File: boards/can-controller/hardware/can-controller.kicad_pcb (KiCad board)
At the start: 2 copper layers, 100 x 100 mm, 5 parts, among them J1 RPi_GPIO

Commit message: can-controller: draft floorplan (Dwgs.User) and edge plan
Connectors: USB-C (GCT USB4085, THT), 12 V MSTB 5.08, CAN1/2 MC 3.5 4p on
the right; relay 10p and analog 12p on the bottom; GPIO 2 x 8p on the
left. 12 V domain bottom right with the isolators on its boundary.

Co-Authored-By: Claude Opus 5.5 <noreply@anthropic.com>
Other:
- board text added: "12 V DOMAIN (CAN bus ground)"
- board text added: "12V IN MSTBA 5.08 2p"
- board text added: "3.3 V LDO (header 5 V)"
- board text added: "ANALOG: AI1-4 + GND x4, AO1-2 + GND x2 MC 3.5 12p"
- board text added: "CAN1 MC 3.5 4p"
- board text added: "CAN1 fuse, TVS, TERM jp"
- board text added: "CAN2 MC 3.5 4p"
- board text added: "CAN2 fuse, TVS, TERM jp"
- board text added: "CAN3/4 expansion header (unpopulated)"
- board text added: "GPIO 1-4 + GND MC 3.5 8p"
- board text added: "GPIO 5-8 + GND MC 3.5 8p (under MCC HAT)"
- board text added: "GPIO series R + clamps"
- board text added: "ISO1042 CAN1"
- board text added: "ISO1042 CAN2"
- board text added: "ISO6741 RLY1-4"
- board text added: "ISO6741 RLY5-8"
- board text added: "LOGIC DOMAIN (Pi ground, header 5 V)"
- board text added: "MCC HAT outline (stacked above)"
- board text added: "PIC32MK1024GPK064 TQFP-64 + crystal"
- board text added: "RELAY 1-8 + 2x 12V COM MC 3.5 10p"
- board text added: "ULN2803A + relay LEDs"
- board text added: "USB ESD, CC 5.1k"
- board text added: "USB-C GCT USB4085 (THT)"
- board text added: "analog: MCP3428 + dividers, DAC + MC34072, boost 15 V, AI/AO protection"
- board text added: "buck 12->5 (ISO bus sides)"
- board text added: "eFuse, TVS, rev. polarity"
- board text added: "opto 12V OK"

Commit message: can-controller: floorplan variant B (4 CAN, Cmts.User) and density estimate
Co-Authored-By: Claude Opus 5.5 <noreply@anthropic.com>
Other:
- board text added: "12 V"
- board text added: "12V IN top-entry MSTBV 5.08 2p"
- board text added: "3.3 V LDO"
- board text added: "ANALOG 12p AI1-4, AO1-2 + GND"
- board text added: "CAN3 MC 3.5 4p"
- board text added: "CAN4 MC 3.5 4p"
- board text added: "GPIO 1-4 MC 3.5 8p"
- board text added: "GPIO 5-8 MC 3.5 8p"
- board text added: "ISO1042 CAN3"
- board text added: "ISO1042 CAN4"
- board text added: "PIC32MK TQFP-64 + crystal"
- board text added: "PTC, TVS, rev-pol FET, buck 12->5"
- board text added: "USB ESD, CC"
- board text added: "USB-C USB4085"
- board text added: "VARIANT B: 4 x CAN (Cmts.User layer)"
- board text added: "analog in/out"
- board text added: "fuse, TVS, TERM jp"
- board text added: "opto 12V"
- board text added: "spare"

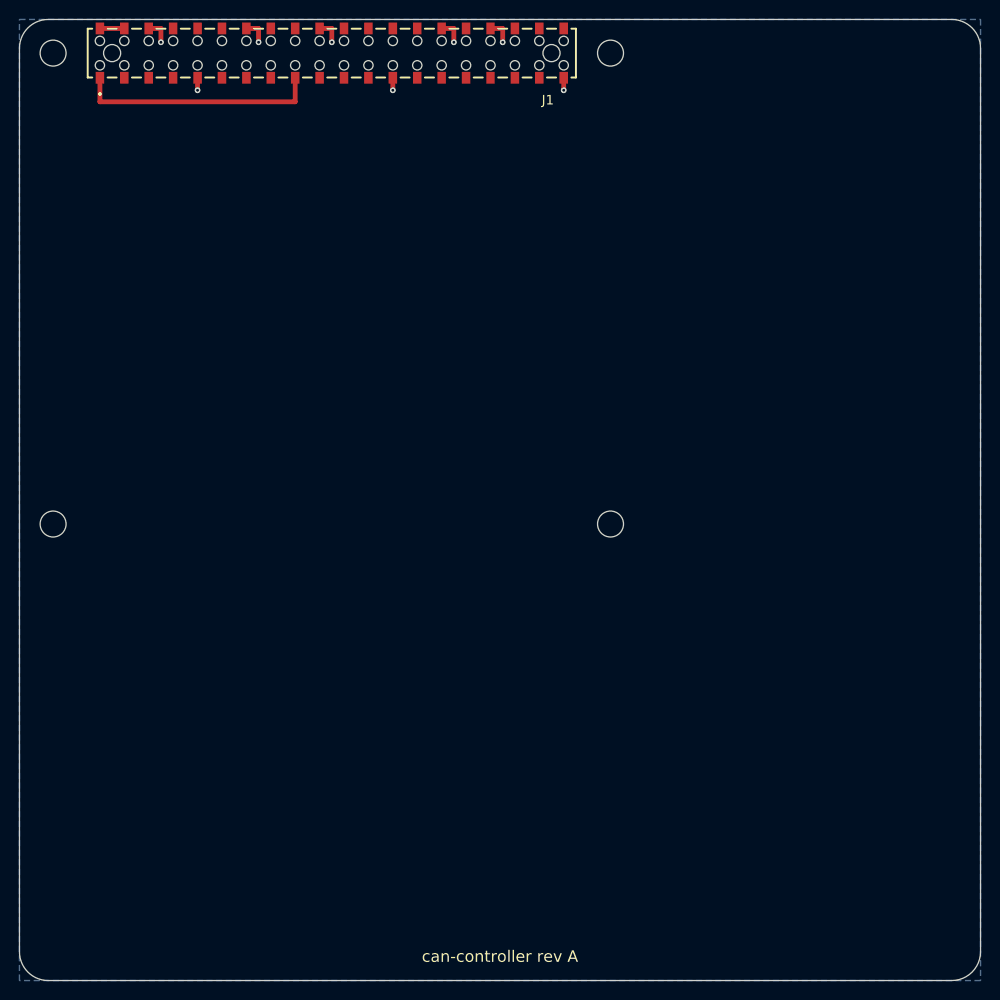
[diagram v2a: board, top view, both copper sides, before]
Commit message: can-controller: floorplan rev 2 (4 CAN), corner holes, DIN clips, draft parts
- Variant B adopted: USB-C + CAN4/3/1/2 on the right edge, 12 V input top
  entry inboard, relay 9p + analog 12p bottom, GPIO 2 x 8p left
- MH5-MH7 M2.5 in the other corners (93 mm square with MH1); DIN clip
  patterns MK1/MK2 at x 125 / 175, as on the first can-ssr layout
- DIN mount footprint: clip body courtyard on B.CrtYd only, 8 mm
  screw-head circles on F.CrtYd
- README: edge table, density estimate, draft parts list (ISO1044BD and
  ISO6740 proposed)

Co-Authored-By: Claude Opus 5.5 <noreply@anthropic.com>
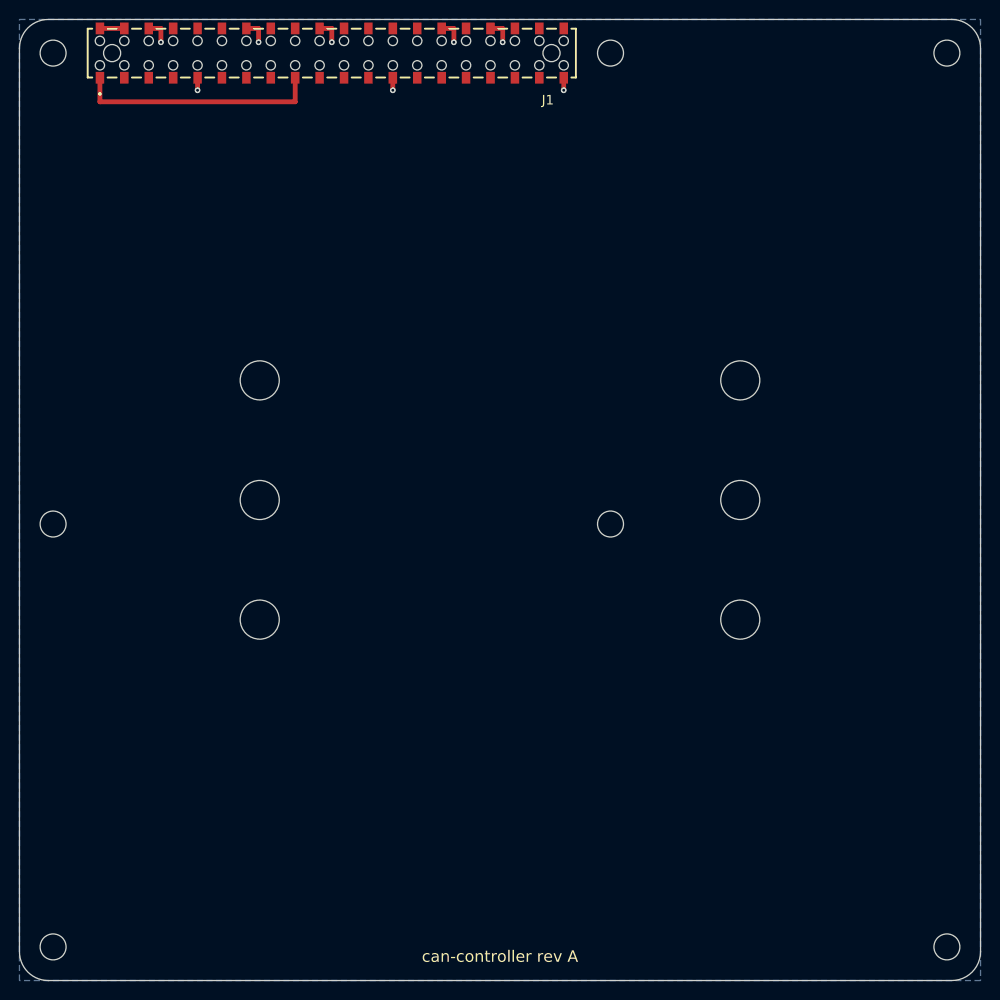
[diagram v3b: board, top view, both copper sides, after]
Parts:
- added MH5: MountingHole_2.7mm_M2.5, MountingHole:MountingHole_2.7mm_M2.5, F.Cu at (196.5, 103.5)
- added MH6: MountingHole_2.7mm_M2.5, MountingHole:MountingHole_2.7mm_M2.5, F.Cu at (103.5, 196.5)
- added MH7: MountingHole_2.7mm_M2.5, MountingHole:MountingHole_2.7mm_M2.5, F.Cu at (196.5, 196.5)
- added MK1: DIN rail clip, Thl_Mechanical:DIN_Rail_Mount_3xNPTH4.06mm_P12.45mm, F.Cu at (125.0, 150.0)
- added MK2: DIN rail clip, Thl_Mechanical:DIN_Rail_Mount_3xNPTH4.06mm_P12.45mm, F.Cu at (175.0, 150.0)
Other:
- board text added: "12 V DOMAIN"
- board text added: "12V IN top-entry MSTBVA 5.08 2p"
- board text added: "3.3 V LDO, ICSP, debug UART"
- board text added: "Floorplan rev 2 (variant B): 4 x CAN, corner holes MH5-7, DIN clips MK1/MK2"
- board text added: "GPIO 5-8 + GND MC 3.5 8p"
- board text added: "ISO1044 CAN1"
- board text added: "ISO1044 CAN2"
- board text added: "ISO1044 CAN3"
- board text added: "ISO1044 CAN4"
- board text added: "ISO6740 RLY1-4"
- board text added: "ISO6740 RLY5-8"
- board text added: "PTC, TVS, TERM jp"
- board text added: "RELAY 1-8 + 12V COM MC 3.5 9p"
- board text added: "ULN2803A SOIC-18W"
- board text added: "USB ESD, CC, LEDs"
- board text added: "analog: MCP3428 + dividers, DAC + op amps + 15 V boost, VREF, AI/AO protection"
- board text added: "buck 12->5"
- board text added: "fuse, TVS, rev-pol FET"
- board text added: "relay + CAN LEDs, 12V status, spare"
- board text removed: "12 V"
- board text removed: "12 V DOMAIN (CAN bus ground)"
- board text removed: "12V IN MSTBA 5.08 2p"
- board text removed: "12V IN top-entry MSTBV 5.08 2p"
- board text removed: "3.3 V LDO"
- board text removed: "3.3 V LDO (header 5 V)"
- board text removed: "ANALOG 12p AI1-4, AO1-2 + GND"
- board text removed: "CAN1 fuse, TVS, TERM jp"
- board text removed: "CAN2 fuse, TVS, TERM jp"
- board text removed: "CAN3/4 expansion header (unpopulated)"
- board text removed: "GPIO 1-4 MC 3.5 8p"
- board text removed: "GPIO 5-8 + GND MC 3.5 8p (under MCC HAT)"
- board text removed: "GPIO 5-8 MC 3.5 8p"
- board text removed: "ISO1042 CAN1"
- board text removed: "ISO1042 CAN2"
- board text removed: "ISO1042 CAN3"
- board text removed: "ISO1042 CAN4"
- board text removed: "ISO6741 RLY1-4"
- board text removed: "ISO6741 RLY5-8"
- board text removed: "MCC HAT outline (stacked above)"
- board text removed: "PIC32MK TQFP-64 + crystal"
- board text removed: "PTC, TVS, rev-pol FET, buck 12->5"
- board text removed: "RELAY 1-8 + 2x 12V COM MC 3.5 10p"
- board text removed: "ULN2803A + relay LEDs"
- board text removed: "USB ESD, CC"
- board text removed: "USB ESD, CC 5.1k"
- board text removed: "USB-C GCT USB4085 (THT)"
- board text removed: "VARIANT B: 4 x CAN (Cmts.User layer)"
- board text removed: "analog in/out"
- board text removed: "analog: MCP3428 + dividers, DAC + MC34072, boost 15 V, AI/AO protection"
- board text removed: "buck 12->5 (ISO bus sides)"
- board text removed: "eFuse, TVS, rev. polarity"
- board text removed: "fuse, TVS, TERM jp"
- board text removed: "opto 12V"
- board text removed: "spare"

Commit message: can-controller: first schematic capture (7 sheets), footprints parked
- gen_schematic.py (first capture only, like can-ssr's): MCU/USB/power,
  CAN x4 (ISO1044BD; +12 V fuse fitted on CAN1, DNP on CAN2-4), 12 V input
  (NANO2 fuse, SUD50P04-08 reverse-polarity P-FET, SMBJ15A, R-78E 5 V for
  the bus sides, TLP293 12 V status), relay drive (2 x ISO6740, ULN2803A,
  logic-side LEDs), GPIO (8 x 4.7k + BAT54S), analog in (MCP3428, dividers
  referenced to VMID because the ADC cannot go below VSS), analog out
  (MCP4922 + LM4040 2.5 V, LM358B gain 4 on a 13 V TPS61040 boost,
  470R + 15 V Zener output protection)
- MCU pin map checked against the PPS group tables of DS60001519E
- ERC 0, parity clean; only isolators span the two domains
- PCB: footprints synced and parked; template copper removed
- sync_pcb.py now carries the DNP attribute to the PCB
- House DRC rule: 0.15 mm annular ring for the GCT USB4085 only
- 3D models for SOIC-4 (SOP-4) and the 1812 PTC (C_1812 stand-in)

Co-Authored-By: Claude Opus 5.5 <noreply@anthropic.com>
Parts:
- added C1: 10uF 25V X7R, Capacitor_SMD:C_1206_3216Metric_Pad1.33x1.80mm_HandSolder, F.Cu at (220.0, 100.0)
- added C10: 27pF 50V C0G, Capacitor_SMD:C_0805_2012Metric_Pad1.18x1.45mm_HandSolder, F.Cu at (245.0, 100.0)
- added C11: 27pF 50V C0G, Capacitor_SMD:C_0805_2012Metric_Pad1.18x1.45mm_HandSolder, F.Cu at (270.0, 100.0)
- added C12: 100nF 50V X7R, Capacitor_SMD:C_0805_2012Metric_Pad1.18x1.45mm_HandSolder, F.Cu at (295.0, 100.0)
- added C2: 10uF 25V X7R, Capacitor_SMD:C_1206_3216Metric_Pad1.33x1.80mm_HandSolder, F.Cu at (320.0, 100.0)
- added C20: 100nF 50V X7R, Capacitor_SMD:C_0805_2012Metric_Pad1.18x1.45mm_HandSolder, F.Cu at (345.0, 100.0)
- added C21: 100nF 50V X7R, Capacitor_SMD:C_0805_2012Metric_Pad1.18x1.45mm_HandSolder, F.Cu at (370.0, 100.0)
- added C22: 100nF 50V X7R, Capacitor_SMD:C_0805_2012Metric_Pad1.18x1.45mm_HandSolder, F.Cu at (395.0, 100.0)
- added C23: 100nF 50V X7R, Capacitor_SMD:C_0805_2012Metric_Pad1.18x1.45mm_HandSolder, F.Cu at (420.0, 100.0)
- added C24: 100nF 50V X7R, Capacitor_SMD:C_0805_2012Metric_Pad1.18x1.45mm_HandSolder, F.Cu at (445.0, 100.0)
- added C25: 100nF 50V X7R, Capacitor_SMD:C_0805_2012Metric_Pad1.18x1.45mm_HandSolder, F.Cu at (220.0, 125.0)
- added C26: 100nF 50V X7R, Capacitor_SMD:C_0805_2012Metric_Pad1.18x1.45mm_HandSolder, F.Cu at (245.0, 125.0)
- added C27: 100nF 50V X7R, Capacitor_SMD:C_0805_2012Metric_Pad1.18x1.45mm_HandSolder, F.Cu at (270.0, 125.0)
- added C3: 100nF 50V X7R, Capacitor_SMD:C_0805_2012Metric_Pad1.18x1.45mm_HandSolder, F.Cu at (295.0, 125.0)
- added C30: 10uF 25V X7R, Capacitor_SMD:C_1206_3216Metric_Pad1.33x1.80mm_HandSolder, F.Cu at (320.0, 125.0)
- added C31: 10uF 25V X7R, Capacitor_SMD:C_1206_3216Metric_Pad1.33x1.80mm_HandSolder, F.Cu at (345.0, 125.0)
- added C32: 10uF 25V X7R, Capacitor_SMD:C_1206_3216Metric_Pad1.33x1.80mm_HandSolder, F.Cu at (370.0, 125.0)
- added C4: 100nF 50V X7R, Capacitor_SMD:C_0805_2012Metric_Pad1.18x1.45mm_HandSolder, F.Cu at (395.0, 125.0)
- added C40: 100nF 50V X7R, Capacitor_SMD:C_0805_2012Metric_Pad1.18x1.45mm_HandSolder, F.Cu at (420.0, 125.0)
- added C41: 100nF 50V X7R, Capacitor_SMD:C_0805_2012Metric_Pad1.18x1.45mm_HandSolder, F.Cu at (445.0, 125.0)
- added C42: 100nF 50V X7R, Capacitor_SMD:C_0805_2012Metric_Pad1.18x1.45mm_HandSolder, F.Cu at (220.0, 150.0)
- added C43: 100nF 50V X7R, Capacitor_SMD:C_0805_2012Metric_Pad1.18x1.45mm_HandSolder, F.Cu at (245.0, 150.0)
- added C44: 10uF 25V X7R, Capacitor_SMD:C_1206_3216Metric_Pad1.33x1.80mm_HandSolder, F.Cu at (270.0, 150.0)
- added C5: 100nF 50V X7R, Capacitor_SMD:C_0805_2012Metric_Pad1.18x1.45mm_HandSolder, F.Cu at (295.0, 150.0)
- added C50: 100nF 50V X7R, Capacitor_SMD:C_0805_2012Metric_Pad1.18x1.45mm_HandSolder, F.Cu at (320.0, 150.0)
- added C51: 10uF 25V X7R, Capacitor_SMD:C_1206_3216Metric_Pad1.33x1.80mm_HandSolder, F.Cu at (345.0, 150.0)
- added C52: 100nF 50V X7R, Capacitor_SMD:C_1206_3216Metric_Pad1.33x1.80mm_HandSolder, F.Cu at (370.0, 150.0)
- added C53: 100nF 50V X7R, Capacitor_SMD:C_1206_3216Metric_Pad1.33x1.80mm_HandSolder, F.Cu at (395.0, 150.0)
- added C54: 100nF 50V X7R, Capacitor_SMD:C_1206_3216Metric_Pad1.33x1.80mm_HandSolder, F.Cu at (420.0, 150.0)
- added C55: 100nF 50V X7R, Capacitor_SMD:C_1206_3216Metric_Pad1.33x1.80mm_HandSolder, F.Cu at (445.0, 150.0)
- added C6: 100nF 50V X7R, Capacitor_SMD:C_0805_2012Metric_Pad1.18x1.45mm_HandSolder, F.Cu at (220.0, 175.0)
- added C60: 100nF 50V X7R, Capacitor_SMD:C_0805_2012Metric_Pad1.18x1.45mm_HandSolder, F.Cu at (245.0, 175.0)
- added C61: 100nF 50V X7R, Capacitor_SMD:C_0805_2012Metric_Pad1.18x1.45mm_HandSolder, F.Cu at (270.0, 175.0)
- added C62: 100nF 50V X7R, Capacitor_SMD:C_0805_2012Metric_Pad1.18x1.45mm_HandSolder, F.Cu at (295.0, 175.0)
- added C63: 4.7uF 25V X7R, Capacitor_SMD:C_1206_3216Metric_Pad1.33x1.80mm_HandSolder, F.Cu at (320.0, 175.0)
- added C64: 10uF 25V X7R, Capacitor_SMD:C_1206_3216Metric_Pad1.33x1.80mm_HandSolder, F.Cu at (345.0, 175.0)
- added C7: 10uF 25V X7R, Capacitor_SMD:C_1206_3216Metric_Pad1.33x1.80mm_HandSolder, F.Cu at (370.0, 175.0)
- added C8: 100nF 50V X7R, Capacitor_SMD:C_0805_2012Metric_Pad1.18x1.45mm_HandSolder, F.Cu at (395.0, 175.0)
- added C9: 100nF 50V X7R, Capacitor_SMD:C_0805_2012Metric_Pad1.18x1.45mm_HandSolder, F.Cu at (420.0, 175.0)
- added D1: LED green, LED_SMD:LED_1206_3216Metric_Pad1.42x1.75mm_HandSolder, F.Cu at (445.0, 175.0)
- added D10: 15V, Diode_SMD:D_SOD-123, F.Cu at (220.0, 200.0)
- added D11: SMBJ15A, Diode_SMD:D_SMB_Handsoldering, F.Cu at (245.0, 200.0)
- added D12: LED green, LED_SMD:LED_1206_3216Metric_Pad1.42x1.75mm_HandSolder, F.Cu at (270.0, 200.0)
- added D2: LED green, LED_SMD:LED_1206_3216Metric_Pad1.42x1.75mm_HandSolder, F.Cu at (295.0, 200.0)
- added D20: NUP2105L, Package_TO_SOT_SMD:SOT-23, F.Cu at (320.0, 200.0)
- added D21: NUP2105L, Package_TO_SOT_SMD:SOT-23, F.Cu at (345.0, 200.0)
- added D22: NUP2105L, Package_TO_SOT_SMD:SOT-23, F.Cu at (370.0, 200.0)
- added D23: NUP2105L, Package_TO_SOT_SMD:SOT-23, F.Cu at (395.0, 200.0)
- added D24: LED yellow, LED_SMD:LED_1206_3216Metric_Pad1.42x1.75mm_HandSolder, F.Cu at (420.0, 200.0)
- added D25: LED yellow, LED_SMD:LED_1206_3216Metric_Pad1.42x1.75mm_HandSolder, F.Cu at (445.0, 200.0)
- added D26: LED yellow, LED_SMD:LED_1206_3216Metric_Pad1.42x1.75mm_HandSolder, F.Cu at (220.0, 225.0)
- added D27: LED yellow, LED_SMD:LED_1206_3216Metric_Pad1.42x1.75mm_HandSolder, F.Cu at (245.0, 225.0)
- added D3: LED green, LED_SMD:LED_1206_3216Metric_Pad1.42x1.75mm_HandSolder, F.Cu at (270.0, 225.0)
- added D31: LED red, LED_SMD:LED_1206_3216Metric_Pad1.42x1.75mm_HandSolder, F.Cu at (295.0, 225.0)
- added D32: LED red, LED_SMD:LED_1206_3216Metric_Pad1.42x1.75mm_HandSolder, F.Cu at (320.0, 225.0)
- added D33: LED red, LED_SMD:LED_1206_3216Metric_Pad1.42x1.75mm_HandSolder, F.Cu at (345.0, 225.0)
- added D34: LED red, LED_SMD:LED_1206_3216Metric_Pad1.42x1.75mm_HandSolder, F.Cu at (370.0, 225.0)
- added D35: LED red, LED_SMD:LED_1206_3216Metric_Pad1.42x1.75mm_HandSolder, F.Cu at (395.0, 225.0)
- added D36: LED red, LED_SMD:LED_1206_3216Metric_Pad1.42x1.75mm_HandSolder, F.Cu at (420.0, 225.0)
- added D37: LED red, LED_SMD:LED_1206_3216Metric_Pad1.42x1.75mm_HandSolder, F.Cu at (445.0, 225.0)
- added D38: LED red, LED_SMD:LED_1206_3216Metric_Pad1.42x1.75mm_HandSolder, F.Cu at (220.0, 250.0)
- added D51: BAT54S, Package_TO_SOT_SMD:SOT-23, F.Cu at (245.0, 250.0)
- added D52: BAT54S, Package_TO_SOT_SMD:SOT-23, F.Cu at (270.0, 250.0)
- added D53: BAT54S, Package_TO_SOT_SMD:SOT-23, F.Cu at (295.0, 250.0)
- added D54: BAT54S, Package_TO_SOT_SMD:SOT-23, F.Cu at (320.0, 250.0)
- added D55: BAT54S, Package_TO_SOT_SMD:SOT-23, F.Cu at (345.0, 250.0)
- added D56: BAT54S, Package_TO_SOT_SMD:SOT-23, F.Cu at (370.0, 250.0)
- added D57: BAT54S, Package_TO_SOT_SMD:SOT-23, F.Cu at (395.0, 250.0)
- added D58: BAT54S, Package_TO_SOT_SMD:SOT-23, F.Cu at (420.0, 250.0)
- added D61: BAT54S, Package_TO_SOT_SMD:SOT-23, F.Cu at (445.0, 250.0)
- added D62: BAT54S, Package_TO_SOT_SMD:SOT-23, F.Cu at (220.0, 275.0)
- added D63: BAT54S, Package_TO_SOT_SMD:SOT-23, F.Cu at (245.0, 275.0)
- added D64: BAT54S, Package_TO_SOT_SMD:SOT-23, F.Cu at (270.0, 275.0)
- added D71: 15V, Diode_SMD:D_SOD-123, F.Cu at (295.0, 275.0)
- added D72: 15V, Diode_SMD:D_SOD-123, F.Cu at (320.0, 275.0)
- added D73: MBR0530, Diode_SMD:D_SOD-123, F.Cu at (345.0, 275.0)
- added F1: 0.75A, Fuse:Fuse_1206_3216Metric_Pad1.42x1.75mm_HandSolder, F.Cu at (370.0, 275.0)
- added F10: 1.1A, Fuse:Fuse_1812_4532Metric_Pad1.30x3.40mm_HandSolder, F.Cu at (395.0, 275.0)
- added F11: 1.1A, Fuse:Fuse_1812_4532Metric_Pad1.30x3.40mm_HandSolder, F.Cu at (420.0, 275.0)
- added F12: 1.1A, Fuse:Fuse_1812_4532Metric_Pad1.30x3.40mm_HandSolder, F.Cu at (445.0, 275.0)
- added F13: 1.1A, Fuse:Fuse_1812_4532Metric_Pad1.30x3.40mm_HandSolder, F.Cu at (220.0, 300.0)
- added F20: 4A, Fuse:Fuse_Littelfuse-NANO2-451_453, F.Cu at (245.0, 300.0)
- added F30: 1.1A, Fuse:Fuse_1812_4532Metric_Pad1.30x3.40mm_HandSolder, F.Cu at (270.0, 300.0)
- added FB1: 600R@100MHz, Inductor_SMD:L_0805_2012Metric_Pad1.05x1.20mm_HandSolder, F.Cu at (295.0, 300.0)
- added J10: CAN1, Connector_Phoenix_MC:PhoenixContact_MC_1,5_4-G-3.5_1x04_P3.50mm_Horizontal, F.Cu at (320.0, 300.0)
- added J11: CAN2, Connector_Phoenix_MC:PhoenixContact_MC_1,5_4-G-3.5_1x04_P3.50mm_Horizontal, F.Cu at (345.0, 300.0)
- added J12: CAN3, Connector_Phoenix_MC:PhoenixContact_MC_1,5_4-G-3.5_1x04_P3.50mm_Horizontal, F.Cu at (370.0, 300.0)
- added J13: CAN4, Connector_Phoenix_MC:PhoenixContact_MC_1,5_4-G-3.5_1x04_P3.50mm_Horizontal, F.Cu at (395.0, 300.0)
- added J2: ICSP, Connector_PinHeader_2.54mm:PinHeader_1x06_P2.54mm_Vertical, F.Cu at (420.0, 300.0)
- added J20: 12V IN, Connector_Phoenix_MSTB:PhoenixContact_MSTBVA_2,5_2-G-5,08_1x02_P5.08mm_Vertical, F.Cu at (445.0, 300.0)
- added J3: UART, Connector_PinHeader_2.54mm:PinHeader_1x03_P2.54mm_Vertical, F.Cu at (220.0, 325.0)
- added J30: RELAY, Connector_Phoenix_MC:PhoenixContact_MC_1,5_9-G-3.5_1x09_P3.50mm_Horizontal, F.Cu at (245.0, 325.0)
- added J4: USB-C, Connector_USB:USB_C_Receptacle_GCT_USB4085, F.Cu at (270.0, 325.0)
- added J40: GPIO 1-4, Connector_Phoenix_MC:PhoenixContact_MC_1,5_8-G-3.5_1x08_P3.50mm_Horizontal, F.Cu at (295.0, 325.0)
- added J41: GPIO 5-8, Connector_Phoenix_MC:PhoenixContact_MC_1,5_8-G-3.5_1x08_P3.50mm_Horizontal, F.Cu at (320.0, 325.0)
- added J50: ANALOG, Connector_Phoenix_MC:PhoenixContact_MC_1,5_12-G-3.5_1x12_P3.50mm_Horizontal, F.Cu at (345.0, 325.0)
- added JP1: TERM, Connector_PinHeader_2.54mm:PinHeader_1x02_P2.54mm_Vertical, F.Cu at (370.0, 325.0)
- added JP2: TERM, Connector_PinHeader_2.54mm:PinHeader_1x02_P2.54mm_Vertical, F.Cu at (395.0, 325.0)
- added JP3: TERM, Connector_PinHeader_2.54mm:PinHeader_1x02_P2.54mm_Vertical, F.Cu at (420.0, 325.0)
- added JP4: TERM, Connector_PinHeader_2.54mm:PinHeader_1x02_P2.54mm_Vertical, F.Cu at (445.0, 325.0)
- added L60: 10uH, Inductor_SMD:L_Bourns-SRN4018, F.Cu at (220.0, 350.0)
- added Q1: SUD50P04-08, Package_TO_SOT_SMD:TO-252-2, F.Cu at (245.0, 350.0)
- added R1: 1k, Resistor_SMD:R_1206_3216Metric_Pad1.30x1.75mm_HandSolder, F.Cu at (270.0, 350.0)
- added R2: 10k, Resistor_SMD:R_1206_3216Metric_Pad1.30x1.75mm_HandSolder, F.Cu at (295.0, 350.0)
- added R20: 120R, Resistor_SMD:R_1206_3216Metric_Pad1.30x1.75mm_HandSolder, F.Cu at (320.0, 350.0)
- added R21: 120R, Resistor_SMD:R_1206_3216Metric_Pad1.30x1.75mm_HandSolder, F.Cu at (345.0, 350.0)
- added R22: 120R, Resistor_SMD:R_1206_3216Metric_Pad1.30x1.75mm_HandSolder, F.Cu at (370.0, 350.0)
- added R23: 120R, Resistor_SMD:R_1206_3216Metric_Pad1.30x1.75mm_HandSolder, F.Cu at (395.0, 350.0)
- added R24: 1k, Resistor_SMD:R_1206_3216Metric_Pad1.30x1.75mm_HandSolder, F.Cu at (420.0, 350.0)
- added R25: 1k, Resistor_SMD:R_1206_3216Metric_Pad1.30x1.75mm_HandSolder, F.Cu at (445.0, 350.0)
- added R26: 1k, Resistor_SMD:R_1206_3216Metric_Pad1.30x1.75mm_HandSolder, F.Cu at (220.0, 375.0)
- added R27: 1k, Resistor_SMD:R_1206_3216Metric_Pad1.30x1.75mm_HandSolder, F.Cu at (245.0, 375.0)
- added R3: 5.1k, Resistor_SMD:R_1206_3216Metric_Pad1.30x1.75mm_HandSolder, F.Cu at (270.0, 375.0)
- added R30: 10k, Resistor_SMD:R_1206_3216Metric_Pad1.30x1.75mm_HandSolder, F.Cu at (295.0, 375.0)
- added R31: 4.7k, Resistor_SMD:R_1206_3216Metric_Pad1.30x1.75mm_HandSolder, F.Cu at (320.0, 375.0)
- added R32: 10k, Resistor_SMD:R_1206_3216Metric_Pad1.30x1.75mm_HandSolder, F.Cu at (345.0, 375.0)
- added R33: 10k, Resistor_SMD:R_1206_3216Metric_Pad1.30x1.75mm_HandSolder, F.Cu at (370.0, 375.0)
- added R34: 1k, Resistor_SMD:R_1206_3216Metric_Pad1.30x1.75mm_HandSolder, F.Cu at (395.0, 375.0)
- added R4: 5.1k, Resistor_SMD:R_1206_3216Metric_Pad1.30x1.75mm_HandSolder, F.Cu at (420.0, 375.0)
- added R41: 1k, Resistor_SMD:R_1206_3216Metric_Pad1.30x1.75mm_HandSolder, F.Cu at (445.0, 375.0)
- added R42: 1k, Resistor_SMD:R_1206_3216Metric_Pad1.30x1.75mm_HandSolder, F.Cu at (220.0, 400.0)
- added R43: 1k, Resistor_SMD:R_1206_3216Metric_Pad1.30x1.75mm_HandSolder, F.Cu at (245.0, 400.0)
- added R44: 1k, Resistor_SMD:R_1206_3216Metric_Pad1.30x1.75mm_HandSolder, F.Cu at (270.0, 400.0)
- added R45: 1k, Resistor_SMD:R_1206_3216Metric_Pad1.30x1.75mm_HandSolder, F.Cu at (295.0, 400.0)
- added R46: 1k, Resistor_SMD:R_1206_3216Metric_Pad1.30x1.75mm_HandSolder, F.Cu at (320.0, 400.0)
- added R47: 1k, Resistor_SMD:R_1206_3216Metric_Pad1.30x1.75mm_HandSolder, F.Cu at (345.0, 400.0)
- added R48: 1k, Resistor_SMD:R_1206_3216Metric_Pad1.30x1.75mm_HandSolder, F.Cu at (370.0, 400.0)
- added R5: 1k, Resistor_SMD:R_1206_3216Metric_Pad1.30x1.75mm_HandSolder, F.Cu at (395.0, 400.0)
- added R51: 4.7k, Resistor_SMD:R_1206_3216Metric_Pad1.30x1.75mm_HandSolder, F.Cu at (420.0, 400.0)
- added R52: 4.7k, Resistor_SMD:R_1206_3216Metric_Pad1.30x1.75mm_HandSolder, F.Cu at (445.0, 400.0)
- added R53: 4.7k, Resistor_SMD:R_1206_3216Metric_Pad1.30x1.75mm_HandSolder, F.Cu at (220.0, 425.0)
- added R54: 4.7k, Resistor_SMD:R_1206_3216Metric_Pad1.30x1.75mm_HandSolder, F.Cu at (245.0, 425.0)
- added R55: 4.7k, Resistor_SMD:R_1206_3216Metric_Pad1.30x1.75mm_HandSolder, F.Cu at (270.0, 425.0)
- added R56: 4.7k, Resistor_SMD:R_1206_3216Metric_Pad1.30x1.75mm_HandSolder, F.Cu at (295.0, 425.0)
- added R57: 4.7k, Resistor_SMD:R_1206_3216Metric_Pad1.30x1.75mm_HandSolder, F.Cu at (320.0, 425.0)
- added R58: 4.7k, Resistor_SMD:R_1206_3216Metric_Pad1.30x1.75mm_HandSolder, F.Cu at (345.0, 425.0)
- added R6: 100k, Resistor_SMD:R_1206_3216Metric_Pad1.30x1.75mm_HandSolder, F.Cu at (370.0, 425.0)
- added R60: 4.7k, Resistor_SMD:R_1206_3216Metric_Pad1.30x1.75mm_HandSolder, F.Cu at (395.0, 425.0)
- added R61: 4.7k, Resistor_SMD:R_1206_3216Metric_Pad1.30x1.75mm_HandSolder, F.Cu at (420.0, 425.0)
- added R62: 10k, Resistor_SMD:R_1206_3216Metric_Pad1.30x1.75mm_HandSolder, F.Cu at (445.0, 425.0)
- added R63: 10k, Resistor_SMD:R_1206_3216Metric_Pad1.30x1.75mm_HandSolder, F.Cu at (220.0, 450.0)
- added R64: 10M, Resistor_SMD:R_1206_3216Metric_Pad1.30x1.75mm_HandSolder, F.Cu at (245.0, 450.0)
- added R65: 10M, Resistor_SMD:R_1206_3216Metric_Pad1.30x1.75mm_HandSolder, F.Cu at (270.0, 450.0)
- added R66: 10M, Resistor_SMD:R_1206_3216Metric_Pad1.30x1.75mm_HandSolder, F.Cu at (295.0, 450.0)
- added R67: 10M, Resistor_SMD:R_1206_3216Metric_Pad1.30x1.75mm_HandSolder, F.Cu at (320.0, 450.0)
- added R68: 130k, Resistor_SMD:R_1206_3216Metric_Pad1.30x1.75mm_HandSolder, F.Cu at (345.0, 450.0)
- added R69: 130k, Resistor_SMD:R_1206_3216Metric_Pad1.30x1.75mm_HandSolder, F.Cu at (370.0, 450.0)
- added R7: 1k, Resistor_SMD:R_1206_3216Metric_Pad1.30x1.75mm_HandSolder, F.Cu at (395.0, 450.0)
- added R70: 130k, Resistor_SMD:R_1206_3216Metric_Pad1.30x1.75mm_HandSolder, F.Cu at (420.0, 450.0)
- added R71: 130k, Resistor_SMD:R_1206_3216Metric_Pad1.30x1.75mm_HandSolder, F.Cu at (445.0, 450.0)
- added R8: 1k, Resistor_SMD:R_1206_3216Metric_Pad1.30x1.75mm_HandSolder, F.Cu at (345.0, 475.0)
- added R80: 1k, Resistor_SMD:R_1206_3216Metric_Pad1.30x1.75mm_HandSolder, F.Cu at (370.0, 475.0)
- added R81: 470R, Resistor_SMD:R_1206_3216Metric_Pad1.30x1.75mm_HandSolder, F.Cu at (395.0, 475.0)
- added R82: 30k, Resistor_SMD:R_1206_3216Metric_Pad1.30x1.75mm_HandSolder, F.Cu at (220.0, 100.0)
- added R83: 10k, Resistor_SMD:R_1206_3216Metric_Pad1.30x1.75mm_HandSolder, F.Cu at (245.0, 100.0)
- added R85: 470R, Resistor_SMD:R_1206_3216Metric_Pad1.30x1.75mm_HandSolder, F.Cu at (270.0, 100.0)
- added R86: 30k, Resistor_SMD:R_1206_3216Metric_Pad1.30x1.75mm_HandSolder, F.Cu at (295.0, 100.0)
- added R87: 10k, Resistor_SMD:R_1206_3216Metric_Pad1.30x1.75mm_HandSolder, F.Cu at (320.0, 100.0)
- added R90: 1M, Resistor_SMD:R_1206_3216Metric_Pad1.30x1.75mm_HandSolder, F.Cu at (345.0, 100.0)
- added R91: 105k, Resistor_SMD:R_1206_3216Metric_Pad1.30x1.75mm_HandSolder, F.Cu at (370.0, 100.0)
- added U1: PIC32MK1024MCM064-I/PT, Package_QFP:TQFP-64_10x10mm_P0.5mm, F.Cu at (420.0, 475.0)
- added U10: ISO1044BD, Package_SO:SOIC-8_3.9x4.9mm_P1.27mm, F.Cu at (445.0, 475.0)
- added U11: ISO1044BD, Package_SO:SOIC-8_3.9x4.9mm_P1.27mm, F.Cu at (220.0, 500.0)
- added U12: ISO1044BD, Package_SO:SOIC-8_3.9x4.9mm_P1.27mm, F.Cu at (245.0, 500.0)
- added U13: ISO1044BD, Package_SO:SOIC-8_3.9x4.9mm_P1.27mm, F.Cu at (270.0, 500.0)
- added U2: MCP1826S-3302E/DB, Package_TO_SOT_SMD:SOT-223-3_TabPin2, F.Cu at (295.0, 500.0)
- added U20: R-78E5.0-0.5, Converter_DCDC:Converter_DCDC_RECOM_R-78E-0.5_THT, F.Cu at (320.0, 500.0)
- added U21: TLP293, Package_SO:SOIC-4_4.55x2.6mm_P1.27mm, F.Cu at (345.0, 500.0)
- added U3: USBLC6-2SC6, Package_TO_SOT_SMD:SOT-23-6, F.Cu at (370.0, 500.0)
- added U30: ISO6740, Package_SO:SOIC-16W_7.5x10.3mm_P1.27mm, F.Cu at (395.0, 500.0)
- added U31: ISO6740, Package_SO:SOIC-16W_7.5x10.3mm_P1.27mm, F.Cu at (420.0, 500.0)
- added U32: ULN2803A, Package_SO:SOIC-18W_7.5x11.6mm_P1.27mm, F.Cu at (445.0, 500.0)
- added U50: MCP3428-E/SL, Package_SO:SOIC-14_3.9x8.7mm_P1.27mm, F.Cu at (220.0, 525.0)
- added U60: MCP4922-E/SL, Package_SO:SOIC-14_3.9x8.7mm_P1.27mm, F.Cu at (245.0, 525.0)
- added U61: LM4040-2.5, Package_TO_SOT_SMD:SOT-23, F.Cu at (270.0, 525.0)
- added U62: LM358B, Package_SO:SOIC-8_3.9x4.9mm_P1.27mm, F.Cu at (295.0, 525.0)
- added U63: TPS61040, Package_TO_SOT_SMD:SOT-23-5, F.Cu at (320.0, 525.0)
- added Y1: 12MHz, Crystal:Crystal_SMD_5032-2Pin_5.0x3.2mm_HandSoldering, F.Cu at (345.0, 525.0)
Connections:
- net +5V renamed /MCU, USB, power/V5_PI
- J1 pad 1: +3.3V -> unconnected-(J1-Pin_1-Pad1)
- J1 pad 10: /GPIO15_RXD -> unconnected-(J1-Pin_10-Pad10)
- J1 pad 11: /GPIO17 -> unconnected-(J1-Pin_11-Pad11)
- J1 pad 12: /GPIO18_PCM_CLK -> unconnected-(J1-Pin_12-Pad12)
- J1 pad 13: /GPIO27 -> unconnected-(J1-Pin_13-Pad13)
- J1 pad 15: /GPIO22 -> unconnected-(J1-Pin_15-Pad15)
- J1 pad 16: /GPIO23 -> unconnected-(J1-Pin_16-Pad16)
- J1 pad 17: +3.3V -> unconnected-(J1-Pin_17-Pad17)
- J1 pad 18: /GPIO24 -> unconnected-(J1-Pin_18-Pad18)
- J1 pad 22: /GPIO25 -> unconnected-(J1-Pin_22-Pad22)
- J1 pad 29: /GPIO5 -> unconnected-(J1-Pin_29-Pad29)
- J1 pad 3: /GPIO2_SDA -> unconnected-(J1-Pin_3-Pad3)
- J1 pad 31: /GPIO6 -> unconnected-(J1-Pin_31-Pad31)
- J1 pad 35: /GPIO19_PCM_FS -> unconnected-(J1-Pin_35-Pad35)
- J1 pad 5: /GPIO3_SCL -> unconnected-(J1-Pin_5-Pad5)
- J1 pad 7: /GPIO4_GPCLK0 -> unconnected-(J1-Pin_7-Pad7)
- J1 pad 8: /GPIO14_TXD -> unconnected-(J1-Pin_8-Pad8)
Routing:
- net +3.3V: track 25.3 -> 0.00 mm
- net GND: track 17.5 -> 0.00 mm, vias 8 -> 0
- net /MCU, USB, power/V5_PI: track 2.54 -> 0.00 mm
- removed copper zone on B.Cu, net GND
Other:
- board text added: "PIC32MK1024MCM064 TQFP-64 + crystal"
- board text removed: "PIC32MK1024GPK064 TQFP-64 + crystal"

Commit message: can-controller: first-pass placement
- place_board.py: fixed edge connectors, MCU and isolators; every other
  part to the nearest free spot by courtyard, domain and keep-outs
- 12 V block extended up to y 146; CAN1/CAN2 isolators on its top edge
- DIN screw keep-outs from the footprint courtyard (r 4 mm)
- USB4085 footprint-scoped clearance and drill-spacing rules (house too)
- Domain boundary redrawn on Dwgs.User
- DRC: only unrouted nets and silkscreen remain

Co-Authored-By: Claude Opus 5.5 <noreply@anthropic.com>
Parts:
- moved U1 448.0 mm to (150.0, 117.5)
- moved Y1 446.6 mm to (161.8, 117.7), turned to 90 degrees
- moved U10 437.2 mm to (158.2, 145.0), turned to -90 degrees
- moved U63 429.2 mm to (152.8, 129.8)
- moved U3 428.9 mm to (185.0, 113.0), turned to 90 degrees
- moved U32 424.7 mm to (163.1, 182.4)
- moved U2 421.6 mm to (130.0, 112.0)
- moved U31 420.0 mm to (148.0, 180.0)
- moved U62 416.8 mm to (149.2, 134.5)
- moved U30 414.4 mm to (148.0, 167.2)
- moved R71 412.8 mm to (133.4, 179.3), turned to 90 degrees
- moved R7 412.5 mm to (172.0, 103.0), turned to 90 degrees
- moved R8 408.6 mm to (176.0, 103.0), turned to 90 degrees
- moved R80 406.7 mm to (120.0, 154.2), turned to 90 degrees
- moved R52 404.9 mm to (114.5, 166.1)
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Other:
- board text added: "12 V DOMAIN (GND_BUS)"
- board text added: "Domain boundary (placement rev 1): only U10-U13, U21, U30, U31 cross it"
- board text added: "LOGIC DOMAIN (GND)"
- board text removed: "12 V DOMAIN"
- board text removed: "12V IN top-entry MSTBVA 5.08 2p"
- board text removed: "3.3 V LDO, ICSP, debug UART"
- board text removed: "ANALOG: AI1-4 + GND x4, AO1-2 + GND x2 MC 3.5 12p"
- board text removed: "CAN1 MC 3.5 4p"
- board text removed: "CAN2 MC 3.5 4p"
- board text removed: "CAN3 MC 3.5 4p"
- board text removed: "CAN4 MC 3.5 4p"
- board text removed: "Floorplan rev 2 (variant B): 4 x CAN, corner holes MH5-7, DIN clips MK1/MK2"
- board text removed: "GPIO 1-4 + GND MC 3.5 8p"
- board text removed: "GPIO 5-8 + GND MC 3.5 8p"
- board text removed: "GPIO series R + clamps"
- board text removed: "ISO1044 CAN1"
- board text removed: "ISO1044 CAN2"
- board text removed: "ISO1044 CAN3"
- board text removed: "ISO1044 CAN4"
- board text removed: "ISO6740 RLY1-4"
- board text removed: "ISO6740 RLY5-8"
- board text removed: "LOGIC DOMAIN (Pi ground, header 5 V)"
- board text removed: "PIC32MK1024MCM064 TQFP-64 + crystal"
- board text removed: "PTC, TVS, TERM jp"
- board text removed: "RELAY 1-8 + 12V COM MC 3.5 9p"
- board text removed: "ULN2803A SOIC-18W"
- board text removed: "USB ESD, CC, LEDs"
- board text removed: "USB-C USB4085"
- board text removed: "analog: MCP3428 + dividers, DAC + op amps + 15 V boost, VREF, AI/AO protection"
- board text removed: "buck 12->5"
- board text removed: "fuse, TVS, rev-pol FET"
- board text removed: "opto 12V OK"
- board text removed: "relay + CAN LEDs, 12V status, spare"
